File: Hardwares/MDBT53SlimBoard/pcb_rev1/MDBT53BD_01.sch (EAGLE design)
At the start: 0 parts

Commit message: 回路図の作成
・時刻同期部を作成
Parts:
- added C1: 0.1uF, Parts:CAP_0402N
- added R1, R2, R3, R4: 10k, Parts:RESISTOR_0402N
- added U1: RV-3028-C7, ICs:RV-3028-C7
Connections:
- new net 0V: C1.2, R3.1, R4.1, U1.VSS
- new net N$2: R3.2, U1.EVI
- new net N$3: R4.2, U1.VBACKUP
- new net TWI_SCL: R2.1, U1.SCL@
- new net TWI_SDA: R1.1, U1.SDA@
- new net VDD_NRF: C1.1, R1.2, R2.2, U1.VDD
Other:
- note added: "LED部"
- note added: "SWDインターフェース部"
- note added: "USBインターフェース部"
- note added: "時刻同期部"
- note added: "電源供給部"
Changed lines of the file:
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@@
 <layer number="56" name="wert" color="7" fill="1" visible="no" active="no"/>
 <layer number="57" name="tCAD" color="7" fill="1" visible="no" active="no"/>
+<layer number="59" name="tCarbon" color="7" fill="1" visible="no" active="no"/>
+<layer number="60" name="bCarbon" color="7" fill="1" visible="no" active="no"/>
 <layer number="90" name="Modules" color="5" fill="1" visible="yes" active="yes"/>
 <layer number="91" name="Nets" color="2" fill="1" visible="yes" active="yes"/>
@@
 <layer number="112" name="tSilk" color="7" fill="1" visible="no" active="yes"/>
 <layer number="113" name="IDFDebug" color="4" fill="1" visible="no" active="yes"/>
+<layer number="114" name="FRNTMAAT1" color="7" fill="1" visible="yes" active="yes"/>
+<layer number="115" name="FRNTMAAT2" color="7" fill="1" visible="yes" active="yes"/>
 <layer number="116" name="Patch_BOT" color="9" fill="4" visible="no" active="yes"/>
+<layer number="117" name="BACKMAAT1" color="7" fill="1" visible="yes" active="yes"/>
+<layer number="118" name="Rect_Pads" color="7" fill="1" visible="no" active="no"/>
+<layer number="119" name="KAP_TEKEN" color="7" fill="1" visible="yes" active="yes"/>
+<layer number="120" name="KAP_MAAT1" color="7" fill="1" visible="yes" active="yes"/>
 <layer number="121" name="_tsilk" color="7" fill="1" visible="no" active="yes"/>
 <layer number="122" name="_bsilk" color="7" fill="1" visible="no" active="yes"/>
@@
 <layer number="127" name="_tValues" color="7" fill="1" visible="no" active="yes"/>
 <layer number="128" name="_bValues" color="7" fill="1" visible="no" active="yes"/>
+<layer number="129" name="top_silk" color="7" fill="1" visible="yes" active="yes"/>
+<layer number="130" name="SMDSTROOK" color="7" fill="1" visible="yes" active="yes"/>
 <layer number="131" name="tAdjust" color="7" fill="1" visible="no" active="yes"/>
 <layer number="132" name="bAdjust" color="7" fill="1" visible="no" active="yes"/>
+<layer number="133" name="bottom_silk" color="7" fill="1" visible="yes" active="yes"/>
 <layer number="144" name="Drill_legend" color="7" fill="1" visible="no" active="yes"/>
 <layer number="150" name="Notes" color="7" fill="1" visible="no" active="yes"/>
@@
 <layer number="223" name="223bmp" color="24" fill="1" visible="no" active="no"/>
 <layer number="224" name="224bmp" color="25" fill="1" visible="no" active="no"/>
+<layer number="225" name="225bmp" color="7" fill="1" visible="yes" active="yes"/>
+<layer number="226" name="226bmp" color="7" fill="1" visible="yes" active="yes"/>
+<layer number="227" name="227bmp" color="7" fill="1" visible="yes" active="yes"/>
+<layer number="228" name="228bmp" color="7" fill="1" visible="yes" active="yes"/>
+<layer number="229" name="229bmp" color="7" fill="1" visible="yes" active="yes"/>
+<layer number="230" name="230bmp" color="7" fill="1" visible="yes" active="yes"/>
+<layer number="231" name="Eagle3D_PG1" color="7" fill="1" visible="yes" active="yes"/>
+<layer number="232" name="Eagle3D_PG2" color="7" fill="1" visible="yes" active="yes"/>
+<layer number="233" name="Eagle3D_PG3" color="7" fill="1" visible="yes" active="yes"/>
 <layer number="248" name="Housing" color="7" fill="1" visible="no" active="yes"/>
 <layer number="249" name="Edge" color="7" fill="1" visible="no" active="yes"/>
@@
 <layer number="251" name="SMDround" color="12" fill="11" visible="no" active="no"/>
 <layer number="254" name="cooling" color="7" fill="1" visible="no" active="yes"/>
+<layer number="255" name="Accent" color="7" fill="1" visible="yes" active="yes"/>
 </layers>
 <schematic xreflabel="%F%N/%S.%C%R" xrefpart="/%S.%C%R">
@@
 <parts>
 <part name="FRAME1" library="Generic" deviceset="A4L-LOC" device=""/>
+<part name="FRAME2" library="Generic" deviceset="A4L-LOC" device=""/>
+<part name="FRAME3" library="Generic" deviceset="A4L-LOC" device=""/>
+<part name="U1" library="ICs" deviceset="RV-3028-C7" device=""/>
+<part name="R1" library="Parts" deviceset="RESISTOR" device="_0402N" value="10k"/>
+<part name="R2" library="Parts" deviceset="RESISTOR" device="_0402N" value="10k"/>
+<part name="R3" library="Parts" deviceset="RESISTOR" device="_0402N" value="10k"/>
+<part name="R4" library="Parts" deviceset="RESISTOR" device="_0402N" value="10k"/>
+<part name="C1" library="Parts" deviceset="CAP" device="_0402N" value="0.1uF"/>
+<part name="GND1" library="Supply" deviceset="0V" device=""/>
 </parts>
 <sheets>
@@
 </nets>
 </sheet>
+<sheet>
+<plain>
+<text x="167.64" y="15.24" size="3.302" layer="91">MDBT53 Slim Board</text>
+<text x="182.88" y="10.16" size="3.175" layer="91">(rev1)</text>
+<text x="217.17" y="20.32" size="1.778" layer="91">MDBT53 evaluation board</text>
+<text x="20.32" y="157.48" size="3.302" layer="91">USBインターフェース部</text>
+<text x="20.32" y="88.9" size="3.302" layer="91">電源供給部</text>
+</plain>
+<instances>
+<instance part="FRAME2" gate="G$1" x="0" y="0"/>
+</instances>
+<busses>
+</busses>
+<nets>
+</nets>
+</sheet>
+<sheet>
+<plain>
+<text x="167.64" y="15.24" size="3.302" layer="91">MDBT53 Slim Board</text>
+<text x="182.88" y="10.16" size="3.175" layer="91">(rev1)</text>
+<text x="217.17" y="20.32" size="1.778" layer="91">MDBT53 evaluation board</text>
+<text x="20.32" y="157.48" size="3.302" layer="91">LED部</text>
+<text x="20.32" y="88.9" size="3.302" layer="91">時刻同期部</text>
+<text x="152.4" y="157.48" size="3.302" layer="91">SWDインターフェース部</text>
+</plain>
+<instances>
+<instance part="FRAME3" gate="G$1" x="0" y="0"/>
+<instance part="U1" gate="G$1" x="76.2" y="55.88"/>
+<instance part="R1" gate="G$1" x="50.8" y="55.88" rot="R90"/>
+<instance part="R2" gate="G$1" x="63.5" y="55.88" rot="R90"/>
+<instance part="R3" gate="G$1" x="139.7" y="40.64" rot="R90"/>
+<instance part="R4" gate="G$1" x="152.4" y="40.64" rot="R90"/>
+<instance part="C1" gate="G$1" x="124.46" y="48.26"/>
+<instance part="GND1" gate="1" x="114.3" y="27.94"/>
+</instances>
+<busses>
+</busses>
+<nets>
+<net name="0V" class="0">
+<segment>
+<pinref part="U1" gate="G$1" pin="VSS"/>
+<pinref part="GND1" gate="1" pin="0V"/>
+<wire x1="106.68" y1="50.8" x2="114.3" y2="50.8" width="0.1524" layer="91"/>
+<wire x1="114.3" y1="50.8" x2="114.3" y2="35.56" width="0.1524" layer="91"/>
+<pinref part="C1" gate="G$1" pin="2"/>
+<wire x1="114.3" y1="35.56" x2="114.3" y2="30.48" width="0.1524" layer="91"/>
+<wire x1="124.46" y1="40.64" x2="124.46" y2="35.56" width="0.1524" layer="91"/>
+<wire x1="124.46" y1="35.56" x2="114.3" y2="35.56" width="0.1524" layer="91"/>
+<junction x="114.3" y="35.56"/>
+<pinref part="R4" gate="G$1" pin="1"/>
+<wire x1="124.46" y1="35.56" x2="139.7" y2="35.56" width="0.1524" layer="91"/>
+<wire x1="139.7" y1="35.56" x2="152.4" y2="35.56" width="0.1524" layer="91"/>
+<wire x1="152.4" y1="35.56" x2="152.4" y2="40.64" width="0.1524" layer="91"/>
+<pinref part="R3" gate="G$1" pin="1"/>
+<wire x1="139.7" y1="40.64" x2="139.7" y2="35.56" width="0.1524" layer="91"/>
+<junction x="139.7" y="35.56"/>
+<junction x="124.46" y="35.56"/>
+</segment>
+</net>
+<net name="VDD_NRF" class="0">
+<segment>
+<pinref part="U1" gate="G$1" pin="VDD"/>
+<pinref part="C1" gate="G$1" pin="1"/>
+<wire x1="106.68" y1="55.88" x2="124.46" y2="55.88" width="0.1524" layer="91"/>
+<wire x1="124.46" y1="55.88" x2="124.46" y2="48.26" width="0.1524" layer="91"/>
+<wire x1="124.46" y1="55.88" x2="124.46" y2="71.12" width="0.1524" layer="91"/>
+<pinref part="R2" gate="G$1" pin="2"/>
+<wire x1="63.5" y1="66.04" x2="63.5" y2="71.12" width="0.1524" layer="91"/>
+<wire x1="63.5" y1="71.12" x2="124.46" y2="71.12" width="0.1524" layer="91"/>
+<pinref part="R1" gate="G$1" pin="2"/>
+<wire x1="124.46" y1="71.12" x2="134.62" y2="71.12" width="0.1524" layer="91"/>
+<wire x1="63.5" y1="71.12" x2="50.8" y2="71.12" width="0.1524" layer="91"/>
+<wire x1="50.8" y1="71.12" x2="50.8" y2="66.04" width="0.1524" layer="91"/>
+<junction x="124.46" y="71.12"/>
+<junction x="63.5" y="71.12"/>
+<junction x="124.46" y="55.88"/>
+<label x="134.62" y="71.12" size="1.778" layer="95" xref="yes"/>
+</segment>
+</net>
+<net name="N$2" class="0">
+<segment>
+<pinref part="U1" gate="G$1" pin="EVI"/>
+<pinref part="R3" gate="G$1" pin="2"/>
+<wire x1="106.68" y1="58.42" x2="139.7" y2="58.42" width="0.1524" layer="91"/>
+<wire x1="139.7" y1="58.42" x2="139.7" y2="50.8" width="0.1524" layer="91"/>
+</segment>
+</net>
+<net name="N$3" class="0">
+<segment>
+<pinref part="U1" gate="G$1" pin="VBACKUP"/>
+<pinref part="R4" gate="G$1" pin="2"/>
+<wire x1="106.68" y1="53.34" x2="152.4" y2="53.34" width="0.1524" layer="91"/>
+<wire x1="152.4" y1="53.34" x2="152.4" y2="50.8" width="0.1524" layer="91"/>
+</segment>
+</net>
+<net name="TWI_SCL" class="0">
+<segment>
+<pinref part="U1" gate="G$1" pin="SCL@"/>
+<pinref part="R2" gate="G$1" pin="1"/>
+<wire x1="73.66" y1="53.34" x2="63.5" y2="53.34" width="0.1524" layer="91"/>
+<wire x1="63.5" y1="53.34" x2="63.5" y2="55.88" width="0.1524" layer="91"/>
+<wire x1="63.5" y1="53.34" x2="40.64" y2="53.34" width="0.1524" layer="91"/>
+<wire x1="40.64" y1="53.34" x2="40.64" y2="58.42" width="0.1524" layer="91"/>
+<label x="40.64" y="58.42" size="1.778" layer="95" rot="R90" xref="yes"/>
+<junction x="63.5" y="53.34"/>
+</segment>
+</net>
+<net name="TWI_SDA" class="0">
+<segment>
+<pinref part="U1" gate="G$1" pin="SDA@"/>
+<pinref part="R1" gate="G$1" pin="1"/>
+<wire x1="73.66" y1="50.8" x2="50.8" y2="50.8" width="0.1524" layer="91"/>
+<wire x1="50.8" y1="50.8" x2="50.8" y2="55.88" width="0.1524" layer="91"/>
+<wire x1="50.8" y1="50.8" x2="35.56" y2="50.8" width="0.1524" layer="91"/>
+<wire x1="35.56" y1="50.8" x2="35.56" y2="58.42" width="0.1524" layer="91"/>
+<label x="35.56" y="58.42" size="1.778" layer="95" rot="R90" xref="yes"/>
+<junction x="50.8" y="50.8"/>
+</segment>
+</net>
+</nets>
+</sheet>

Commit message: 回路図の作成
・LED部、SWD I/F部を追加
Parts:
- added CN1: IF_6PIN, Connectors:IF_6PIN
- added D1: APTD1608LSECK/J4-PF, Parts:APTD1608LSECK/J4-PF
- added D2: APHD1608LSURCK, Parts:APHD1608LSURCK
- added D3: APTD1608LZGCK, Parts:APTD1608LZGCK
- added D4: APTD1608LVBC/D, Parts:APTD1608LVBC/D
- added R5, R6: 1.2k, Parts:RESISTOR_0402N
- added R7: 1.5k, Parts:RESISTOR_0402N
- added R8: 390, Parts:RESISTOR_0402N
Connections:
- new net LED1: R5.1
- new net LED2: R6.1
- new net LED3: R7.1
- new net LED4: R8.1
- new net N$1: D1.C, R5.2
- new net N$4: D2.C, R6.2
- new net N$5: D3.C, R7.2
- new net N$6: D4.C, R8.2
- new net RESET: CN1.5
- new net SWDCLK: CN1.4
- new net SWDIO: CN1.3
- new net TXD: CN1.6
- net 0V: now also CN1.1
- net VDD_NRF: now also CN1.2, D1.A, D2.A, D3.A, D4.A
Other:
- note added: "LED（緑色）"
- note added: "LED（赤色）"
- note added: "LED（青色）"
- note added: "LED（黄色）"
- moved on the sheet: C1, R1, R2, R3, R4, U1

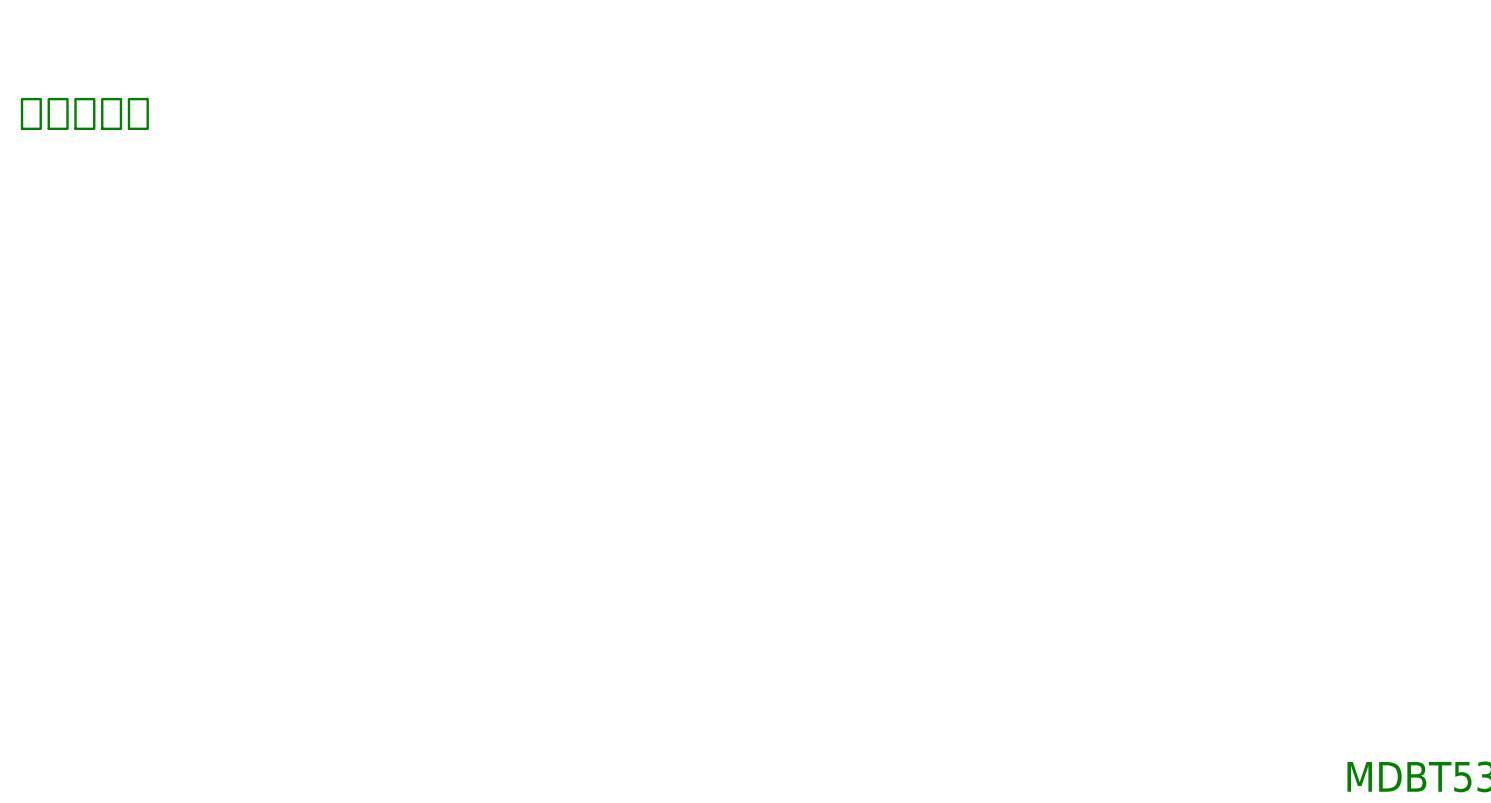
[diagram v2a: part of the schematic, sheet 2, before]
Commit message: 回路図の作成
・電源供給部を追加
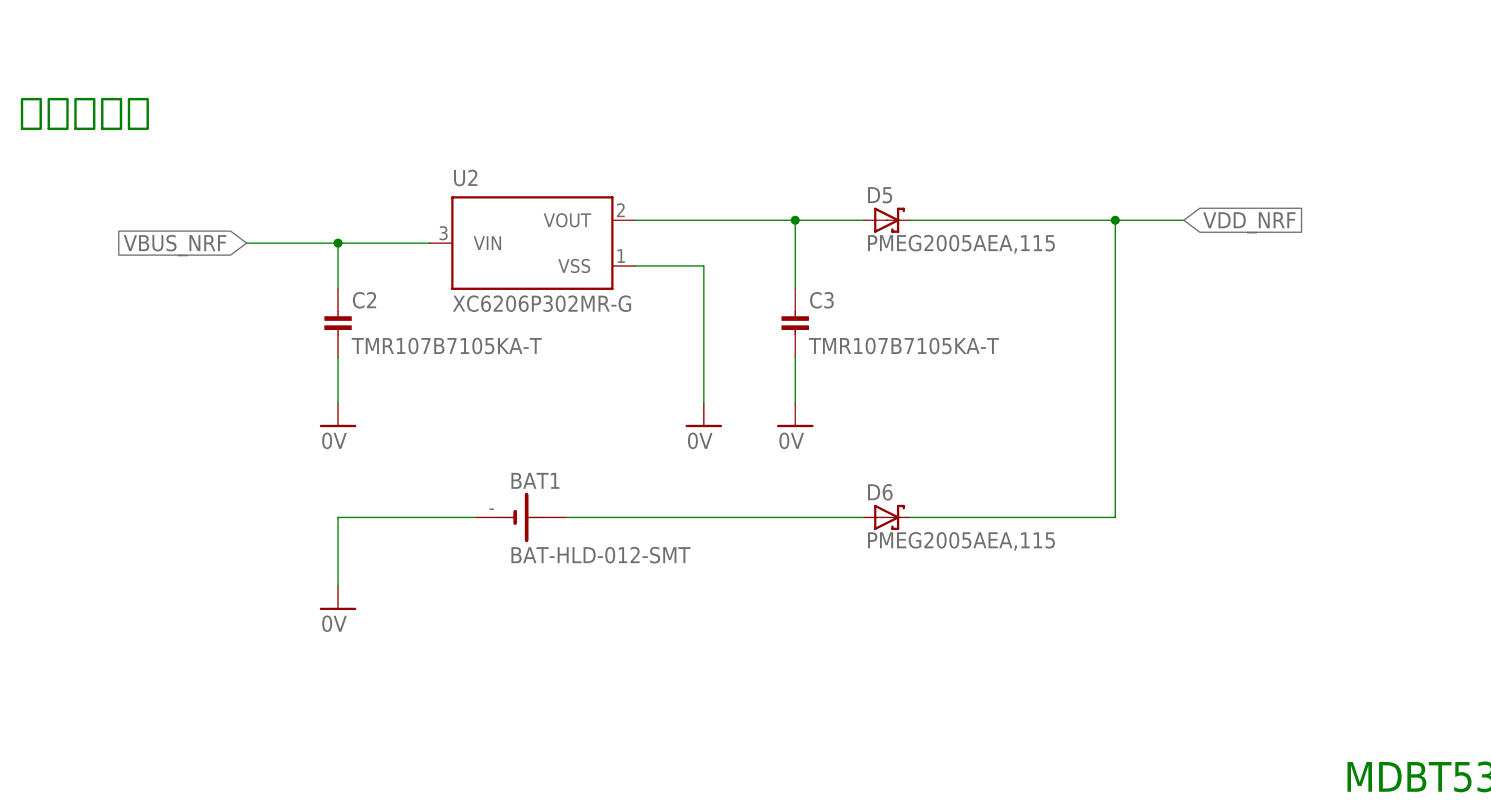
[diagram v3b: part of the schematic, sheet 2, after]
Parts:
- added BAT1: BAT-HLD-012-SMT, Connectors:BAT-HLD-012-SMT
- added C2, C3: TMR107B7105KA-T, Parts:CAP_0603N
- added D5, D6: PMEG2005AEA,115, Parts:PMEG2005AEA,115
- added U2: XC6206P302MR-G, Parts:XC6206P302MR-G
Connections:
- new net N$8: C3.1, D5.A, U2.VOUT
- new net N$9: BAT1.+, D6.A
- new net VBUS_NRF: C2.1, U2.VIN
- net 0V: now also BAT1.-, C2.2, C3.2, U2.VSS
- net VDD_NRF: now also D5.C, D6.C
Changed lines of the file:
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@@
 <part name="R7" library="Parts" deviceset="RESISTOR" device="_0402N" value="1.5k"/>
 <part name="R8" library="Parts" deviceset="RESISTOR" device="_0402N" value="390"/>
+<part name="U2" library="Parts" deviceset="XC6206" device="P302MR-G"/>
+<part name="C2" library="Parts" deviceset="CAP" device="_0603N" value="TMR107B7105KA-T"/>
+<part name="C3" library="Parts" deviceset="CAP" device="_0603N" value="TMR107B7105KA-T"/>
+<part name="D5" library="Parts" deviceset="PMEG2005" device="AEA,115"/>
+<part name="D6" library="Parts" deviceset="PMEG2005" device="AEA,115"/>
+<part name="BAT1" library="Connectors" deviceset="BAT-HLD-012-SMT" device=""/>
+<part name="GND3" library="Supply" deviceset="0V" device=""/>
+<part name="GND4" library="Supply" deviceset="0V" device=""/>
+<part name="GND5" library="Supply" deviceset="0V" device=""/>
+<part name="GND6" library="Supply" deviceset="0V" device=""/>
 </parts>
 <sheets>
@@
 <instances>
 <instance part="FRAME2" gate="G$1" x="0" y="0"/>
+<instance part="U2" gate="G$1" x="66.04" y="78.74"/>
+<instance part="C2" gate="G$1" x="55.88" y="71.12"/>
+<instance part="C3" gate="G$1" x="106.68" y="71.12"/>
+<instance part="D5" gate="G$1" x="116.84" y="78.74"/>
+<instance part="D6" gate="G$1" x="116.84" y="45.72"/>
+<instance part="BAT1" gate="G$1" x="76.2" y="45.72"/>
+<instance part="GND3" gate="1" x="55.88" y="55.88"/>
+<instance part="GND4" gate="1" x="55.88" y="35.56"/>
+<instance part="GND5" gate="1" x="96.52" y="55.88"/>
+<instance part="GND6" gate="1" x="106.68" y="55.88"/>
 </instances>
 <busses>
 </busses>
 <nets>
+<net name="VBUS_NRF" class="0">
+<segment>
+<pinref part="U2" gate="G$1" pin="VIN"/>
+<wire x1="66.04" y1="76.2" x2="55.88" y2="76.2" width="0.1524" layer="91"/>
+<pinref part="C2" gate="G$1" pin="1"/>
+<wire x1="55.88" y1="76.2" x2="45.72" y2="76.2" width="0.1524" layer="91"/>
+<wire x1="55.88" y1="71.12" x2="55.88" y2="76.2" width="0.1524" layer="91"/>
+<label x="45.72" y="76.2" size="1.778" layer="95" rot="R180" xref="yes"/>
+<junction x="55.88" y="76.2"/>
+</segment>
+</net>
+<net name="0V" class="0">
+<segment>
+<pinref part="BAT1" gate="G$1" pin="-"/>
+<pinref part="GND4" gate="1" pin="0V"/>
+<wire x1="71.12" y1="45.72" x2="55.88" y2="45.72" width="0.1524" layer="91"/>
+<wire x1="55.88" y1="45.72" x2="55.88" y2="38.1" width="0.1524" layer="91"/>
+</segment>
+<segment>
+<pinref part="C2" gate="G$1" pin="2"/>
+<pinref part="GND3" gate="1" pin="0V"/>
+<wire x1="55.88" y1="63.5" x2="55.88" y2="58.42" width="0.1524" layer="91"/>
+</segment>
+<segment>
+<pinref part="U2" gate="G$1" pin="VSS"/>
+<pinref part="GND5" gate="1" pin="0V"/>
+<wire x1="88.9" y1="73.66" x2="96.52" y2="73.66" width="0.1524" layer="91"/>
+<wire x1="96.52" y1="73.66" x2="96.52" y2="58.42" width="0.1524" layer="91"/>
+</segment>
+<segment>
+<pinref part="C3" gate="G$1" pin="2"/>
+<pinref part="GND6" gate="1" pin="0V"/>
+<wire x1="106.68" y1="63.5" x2="106.68" y2="58.42" width="0.1524" layer="91"/>
+</segment>
+</net>
+<net name="N$8" class="0">
+<segment>
+<pinref part="U2" gate="G$1" pin="VOUT"/>
+<pinref part="D5" gate="G$1" pin="A"/>
+<wire x1="88.9" y1="78.74" x2="106.68" y2="78.74" width="0.1524" layer="91"/>
+<pinref part="C3" gate="G$1" pin="1"/>
+<wire x1="106.68" y1="78.74" x2="114.3" y2="78.74" width="0.1524" layer="91"/>
+<wire x1="106.68" y1="71.12" x2="106.68" y2="78.74" width="0.1524" layer="91"/>
+<junction x="106.68" y="78.74"/>
+</segment>
+</net>
+<net name="N$9" class="0">
+<segment>
+<pinref part="BAT1" gate="G$1" pin="+"/>
+<pinref part="D6" gate="G$1" pin="A"/>
+<wire x1="81.28" y1="45.72" x2="114.3" y2="45.72" width="0.1524" layer="91"/>
+</segment>
+</net>
+<net name="VDD_NRF" class="0">
+<segment>
+<pinref part="D5" gate="G$1" pin="C"/>
+<wire x1="119.38" y1="78.74" x2="142.24" y2="78.74" width="0.1524" layer="91"/>
+<pinref part="D6" gate="G$1" pin="C"/>
+<wire x1="119.38" y1="45.72" x2="142.24" y2="45.72" width="0.1524" layer="91"/>
+<wire x1="142.24" y1="45.72" x2="142.24" y2="78.74" width="0.1524" layer="91"/>
+<wire x1="142.24" y1="78.74" x2="149.86" y2="78.74" width="0.1524" layer="91"/>
+<label x="149.86" y="78.74" size="1.778" layer="95" xref="yes"/>
+<junction x="142.24" y="78.74"/>
+</segment>
+</net>
 </nets>
 </sheet>

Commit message: 回路図の作成
・USBインターフェース部を追加
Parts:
- added C4: C0603C106M8PACTU, Parts:CAP_0603N
- added C5: C0402C103K5RAC7411, Parts:CAP_0402N
- added C6, C7: UMK105B7104KV-FR, Parts:CAP_0402N
- added CN2: USB4105-GF-A, Connectors:USB4105-GF-A
- added D7: PRTR5V0U2X, Parts:PRTR5V0U2X
- added FB1, FB2, FB3, FB4: BLM15AG121SN1D, Parts:BLM15AG121SN1D
- added R10, R9: CRCW04025K10FKED, Parts:RESISTOR_0402N
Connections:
- new net D_N: CN2.D_N1, CN2.D_N2, D7.I/O_1
- new net D_P: CN2.D_P1, CN2.D_P2, D7.I/O_2
- new net N$10: CN2.CC1, R9.1
- new net N$11: CN2.FG1, CN2.FG2, CN2.FG3, CN2.FG4, FB4.1
- new net N$12: CN2.GND1, CN2.GND2, FB3.1
- new net N$17: C4.1, C5.1, C7.1, CN2.VBUS1, CN2.VBUS2, D7.VCC, FB1.1, FB2.1
- new net N$7: CN2.CC2, R10.1
- new net VBUS_LDO: C2.1, FB1.2, U2.VIN
- net 0V: now also C4.2, C5.2, C6.2, C7.2, D7.GND, FB3.2, FB4.2, R10.2, R9.2
- net VBUS_NRF: now also C6.1, FB2.2; no longer C2.1, U2.VIN
